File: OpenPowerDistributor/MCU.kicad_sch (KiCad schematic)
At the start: 1 part, among them U3 ESP32-S2-WROVER

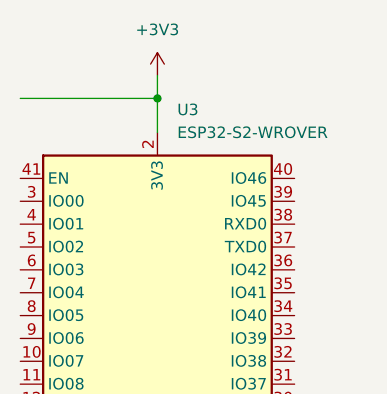
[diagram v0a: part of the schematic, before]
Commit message: Start to make layout
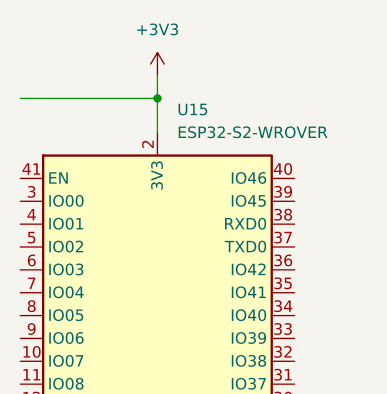
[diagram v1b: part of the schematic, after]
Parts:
- renumbered U3 to U15
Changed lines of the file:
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@@
   (symbol (lib_id "power:+3V3") (at 148.59 33.02 0) (unit 1)
     (in_bom yes) (on_board yes) (dnp no) (fields_autoplaced)
-    (property "Reference" "#PWR020" (at 148.59 36.83 0)
+    (property "Reference" "#PWR0220" (at 148.59 36.83 0)
       (effects (font (size 1.27 1.27)) hide)
     )
@@
       (project "OpenPowerDistribution"
         (path "/df87b081-37a2-452c-8581-7eff2c408a17/9bf24cd5-de70-4a0d-bccf-b175515df8e6"
-          (reference "#PWR020") (unit 1)
+          (reference "#PWR0220") (unit 1)
         )
       )
@@
   (symbol (lib_id "RF_Module:ESP32-S2-WROVER") (at 148.59 69.85 0) (unit 1)
     (in_bom yes) (on_board yes) (dnp no) (fields_autoplaced)
-    (property "Reference" "U3" (at 150.7841 36.83 0)
+    (property "Reference" "U15" (at 150.7841 36.83 0)
       (effects (font (size 1.27 1.27)) (justify left))
     )
@@
       (project "OpenPowerDistribution"
         (path "/df87b081-37a2-452c-8581-7eff2c408a17/9bf24cd5-de70-4a0d-bccf-b175515df8e6"
-          (reference "U3") (unit 1)
+          (reference "U15") (unit 1)
         )
       )
@@
   (symbol (lib_id "power:GND") (at 148.59 97.79 0) (unit 1)
     (in_bom yes) (on_board yes) (dnp no) (fields_autoplaced)
-    (property "Reference" "#PWR019" (at 148.59 104.14 0)
+    (property "Reference" "#PWR0221" (at 148.59 104.14 0)
       (effects (font (size 1.27 1.27)) hide)
     )
@@
       (project "OpenPowerDistribution"
         (path "/df87b081-37a2-452c-8581-7eff2c408a17/9bf24cd5-de70-4a0d-bccf-b175515df8e6"
-          (reference "#PWR019") (unit 1)
+          (reference "#PWR0221") (unit 1)
         )
       )

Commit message: Analog multiplexer work
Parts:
- added D7: SS36(F), Diode_SMD:D_SMA, symbol Device:D_Schottky
- added J2: USB_C_Receptacle_USB2.0, Connector_USB:USB_C_Receptacle_HCTL_HC-TYPE-C-16P-01A, symbol Connector:USB_C_Receptacle_USB2.0
- added R19 (x3): 10k, Resistor_SMD:R_0603_1608Metric, symbol Device:R_Small
- added R20, R21: 5.1k, Resistor_SMD:R_0603_1608Metric, symbol Device:R_Small
- added SW1: BOOT, Button_Switch_SMD:SW_SPST_TL3342, symbol Switch:SW_Push
- added SW1: RST, Button_Switch_SMD:SW_SPST_TL3342, symbol Switch:SW_Push
- added U8: USBLC6-2SC6, Package_TO_SOT_SMD:SOT-23-6, symbol Power_Protection:USBLC6-2SC6
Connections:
- net +3V3: now also R19.1, R19.1
- net GND: now also J2.A1 (GND), J2.A12 (GND), J2.B1 (GND), J2.B12 (GND), J2.S1 (SHIELD), R19.1, R20.1, R21.1, SW1.1, SW1.1, U8.2 (GND)
- net USB-D-: now reaches U15.22 (USB_D-)
- net USB-D-: now also J2.A7 (D-), J2.B7 (D-), U8.3 (I/O2), U8.4 (I/O2)
- net USB-D+: now reaches U15.23 (USB_D+)
- net USB-D+: now also J2.A6 (D+), J2.B6 (D+), U8.1 (I/O1), U8.6 (I/O1)
- net at U15.3 (IO00): now also R19.2, SW1.2
- net ESP32-~{RST}: now reaches U15.41 (EN)
- net ESP32-~{RST}: now also R19.2, SW1.2
- net at U15.5 (IO02): now also R19.2
- net AIN1: now reaches U15.6 (IO03)
- net AIN2: now reaches U15.7 (IO04)
- new net: J2.A5 (CC1), R20.2
- new net: J2.B5 (CC2), R21.2
- new net +12V: D7.1 (K)
- new net VUSB: D7.2 (A), J2.A4 (VBUS), J2.A9 (VBUS), J2.B4 (VBUS), J2.B9 (VBUS), U8.5 (VBUS)
- no-connect marks 0 -> 2
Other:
- note added: "BOOT relevant"
- note added: "Boot behaviour GPIO0 (internal pull-up) SPI boot = 1 Download boot = 0 GPIO2 (internal pull-down) SPI boot = don't care Download boot = 0"
- note added: "Power PoE from USB if not PoE-powered This will also power 3.3V"
- note added: "USB Type-C receptacle"
- note added: "USB overvoltage protection"
- moved on the sheet: U15

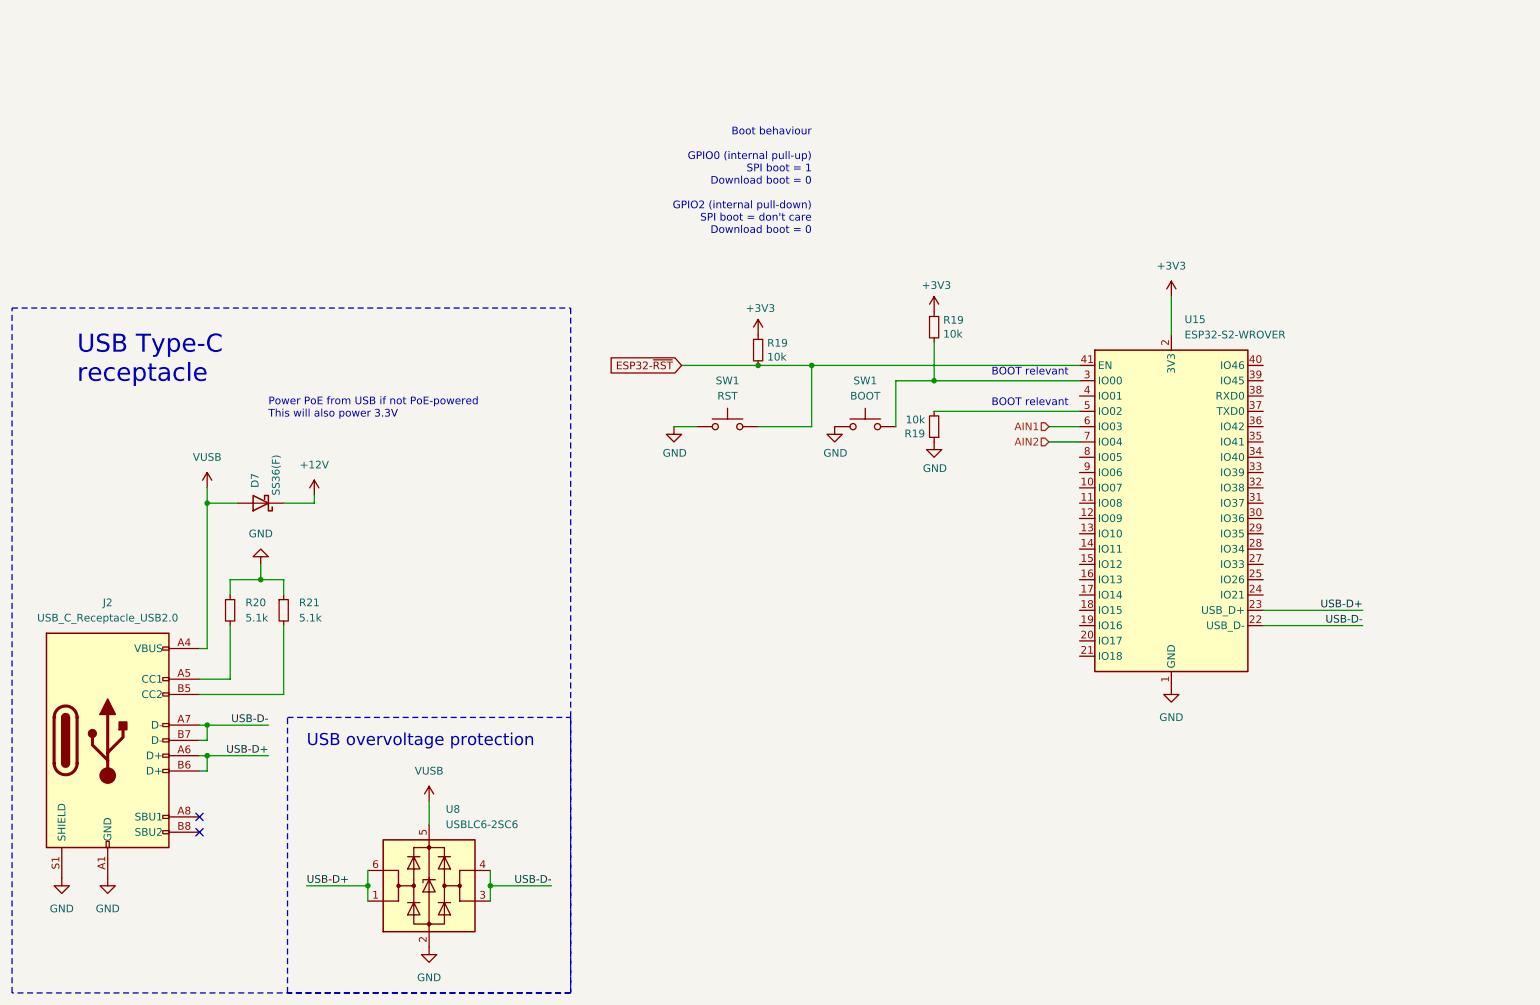
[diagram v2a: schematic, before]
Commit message: Work mostly on Ethernet schematic
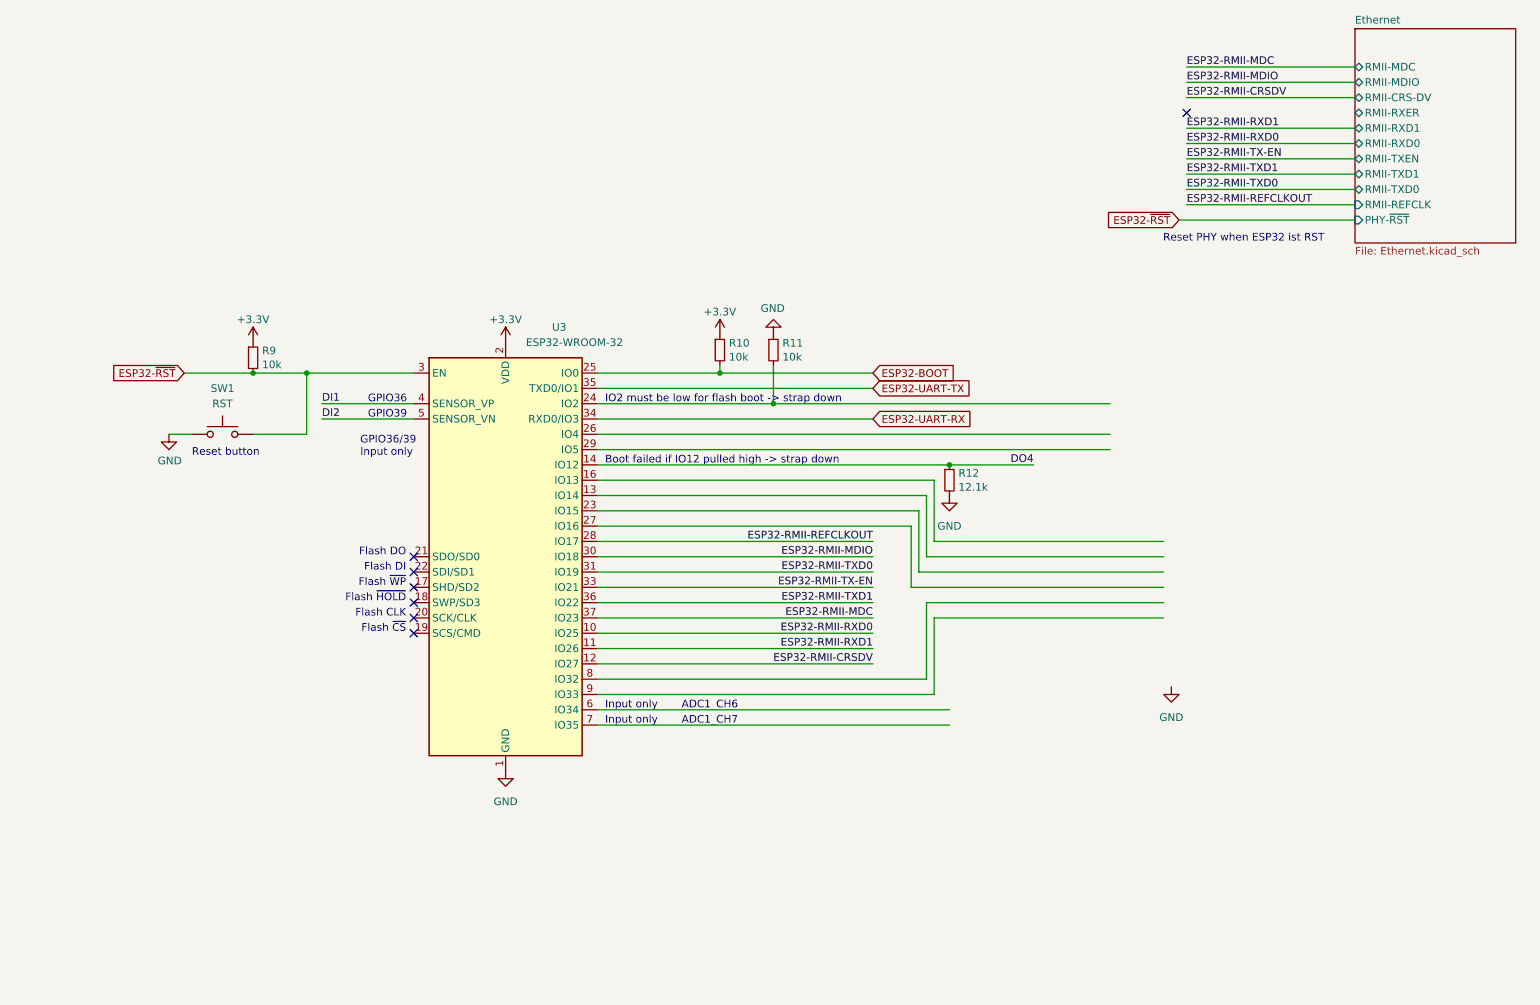
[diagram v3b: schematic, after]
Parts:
- removed D7: SS36(F), Diode_SMD:D_SMA, symbol Device:D_Schottky
- removed J2: USB_C_Receptacle_USB2.0, Connector_USB:USB_C_Receptacle_HCTL_HC-TYPE-C-16P-01A, symbol Connector:USB_C_Receptacle_USB2.0
- removed R19 (x3): 10k, Resistor_SMD:R_0603_1608Metric, symbol Device:R_Small
- removed R20, R21: 5.1k, Resistor_SMD:R_0603_1608Metric, symbol Device:R_Small
- removed SW1: BOOT, Button_Switch_SMD:SW_SPST_TL3342, symbol Switch:SW_Push
- removed SW1: RST, Button_Switch_SMD:SW_SPST_TL3342, symbol Switch:SW_Push
- removed U15: ESP32-S2-WROVER, RF_Module:ESP32-S2-WROVER, symbol RF_Module:ESP32-S2-WROVER
- removed U8: USBLC6-2SC6, Package_TO_SOT_SMD:SOT-23-6, symbol Power_Protection:USBLC6-2SC6
- added R10, R11, R9: 10k, Resistor_SMD:R_0603_1608Metric, symbol Device:R_Small
- added R12: 12.1k, Resistor_SMD:R_0603_1608Metric, symbol Device:R_Small
- added SW1: RST, Button_Switch_SMD:SW_SPST_TL3342, symbol Switch:SW_Push
- added U3: ESP32-WROOM-32, RF_Module:ESP32-WROOM-32D, symbol RF_Module:ESP32-WROOM-32U
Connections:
- net ESP32-~{RST}: now also R9.2, SW1.2, U3.3 (EN)
- net GND: now also R11.1, R12.2, SW1.1, U3.1 (GND), U3.15 (GND), U3.38 (GND), U3.39 (GND)
- new net: R11.2, U3.24 (IO2)
- new net +3.3V: R10.1, R9.1, U3.2 (VDD)
- new net DI1: U3.4 (SENSOR_VP)
- new net DI2: U3.5 (SENSOR_VN)
- new net DO4: R12.1, U3.14 (IO12)
- new net ESP32-BOOT: R10.2, U3.25 (IO0)
- new net ESP32-RMII-CRSDV: U3.12 (IO27)
- new net ESP32-RMII-MDC: U3.37 (IO23)
- new net ESP32-RMII-MDIO: U3.30 (IO18)
- new net ESP32-RMII-REFCLKOUT: U3.28 (IO17)
- new net ESP32-RMII-RXD0: U3.10 (IO25)
- new net ESP32-RMII-RXD1: U3.11 (IO26)
- new net ESP32-RMII-TX-EN: U3.33 (IO21)
- new net ESP32-RMII-TXD0: U3.31 (IO19)
- new net ESP32-RMII-TXD1: U3.36 (IO22)
- new net ESP32-UART-RX: U3.34 (RXD0/IO3)
- new net ESP32-UART-TX: U3.35 (TXD0/IO1)
- no-connect marks 2 -> 7
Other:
- added sheet Ethernet (Ethernet.kicad_sch)
- note added: "ADC1_CH6"
- note added: "ADC1_CH7"
- note added: "Boot failed if IO12 pulled high -> strap down"
- note added: "Flash CLK"
- note added: "Flash DI"
- note added: "Flash DO"
- note added: "Flash ~{CS}"
- note added: "Flash ~{HOLD}"
- note added: "Flash ~{WP}"
- note added: "GPIO36"
- note added: "GPIO36/39 Input only"
- note added: "GPIO39"
- note added: "IO2 must be low for flash boot -> strap down"
- note added: "Input only"
- note added: "Reset PHY when ESP32 ist RST"
- note added: "Reset button"
- note removed: "BOOT relevant"
- note removed: "Boot behaviour GPIO0 (internal pull-up) SPI boot = 1 Download boot = 0 GPIO2 (internal pull-down) SPI boot = don't care Download boot = 0"
- note removed: "Power PoE from USB if not PoE-powered This will also power 3.3V"
- note removed: "USB Type-C receptacle"
- note removed: "USB overvoltage protection"
